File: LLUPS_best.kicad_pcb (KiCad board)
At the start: 2 copper layers, 140 x 90 mm, 39 parts, among them J1 USB_C, J2 Output, J3 Debug, Q1 FS8205A, U1 USBLC6-2SC6, U2 BQ24072, U3 HY2113-KB5B, U4 MT3608, U5 AP2112K-3.3, U6 LN61CN3302MR-G

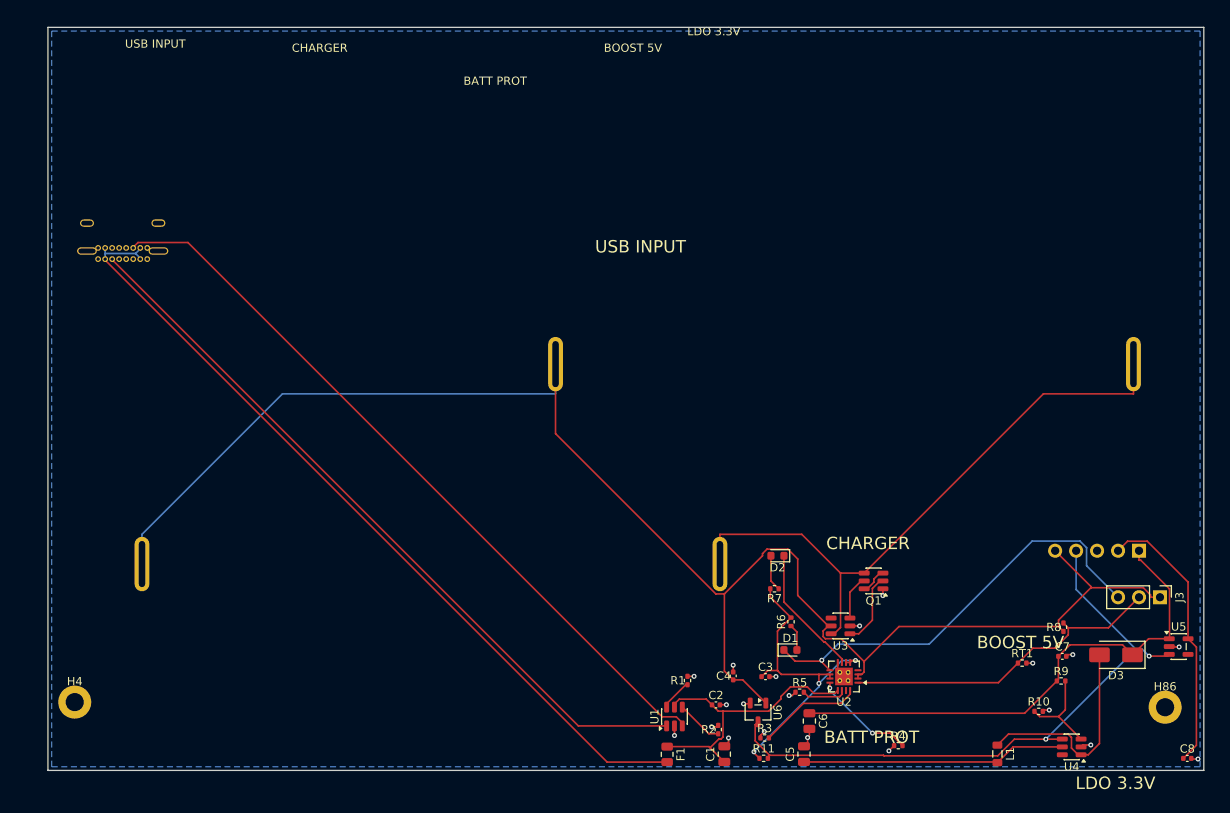
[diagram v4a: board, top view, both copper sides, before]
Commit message: fix: edge connector 180° rotation error on B.Cu (back layer)
When THT connectors are flipped to B.Cu by _assign_layers(), KiCad's
Flip() mirrors the local X-axis. _best_rotation_for_edge() was using
F.Cu outward direction assumptions regardless of layer, causing the
USB connector opening to face inward (toward the board) instead of
outward.

Fix: swap left/right outward angles when comp.layer == Layer.BACK.

Also fix unrelated UnboundLocalError for stop_mid_batch in single-worker
experiment mode.
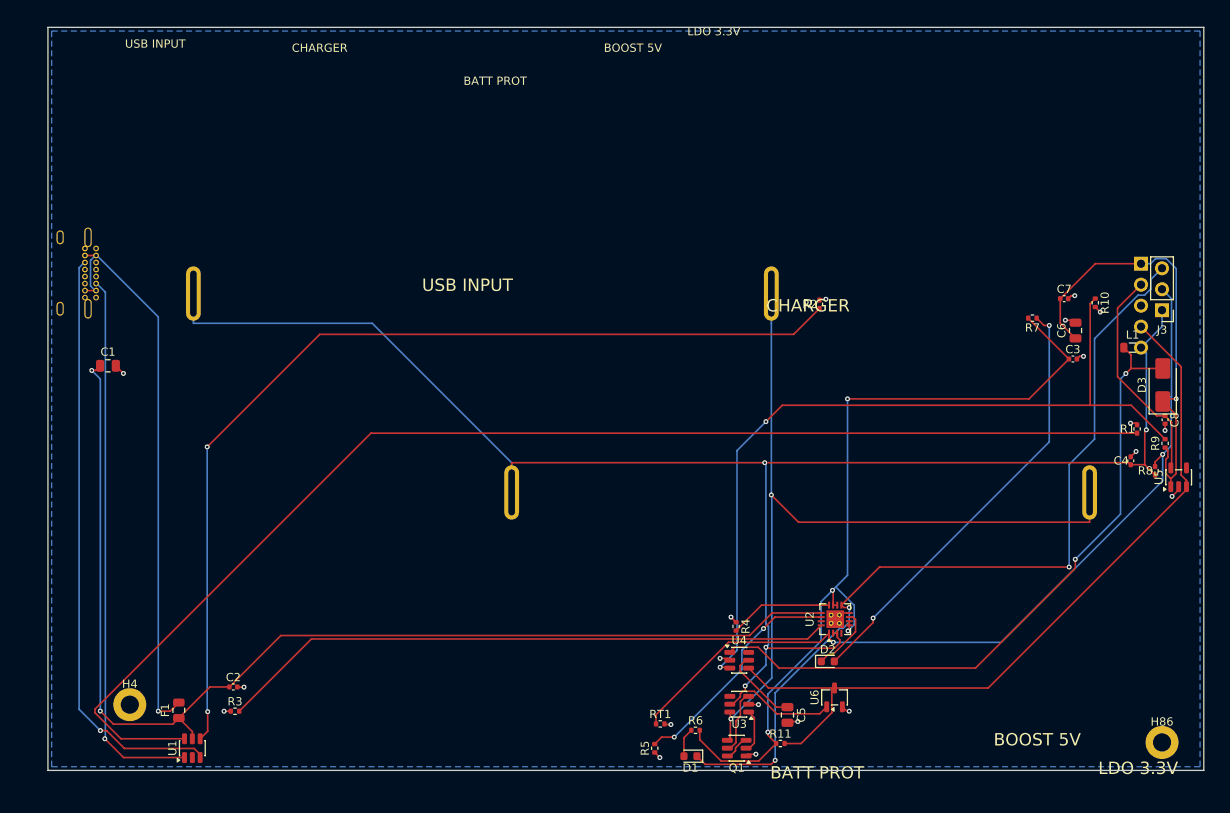
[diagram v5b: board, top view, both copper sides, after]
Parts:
- moved C1 88.2 mm to (7.27, 41.0), turned to 0 degrees
- moved R3 64.2 mm to (22.7, 82.8)
- moved R1 62.4 mm to (131.9, 48.6)
- moved F1 59.4 mm to (15.9, 82.7), turned to 90 degrees
- moved U1 58.5 mm to (17.5, 87.3)
- moved C2 58.5 mm to (22.5, 79.9)
- moved C6 57.2 mm to (124.5, 36.7), turned to 90 degrees
- moved C4 54.8 mm to (131.2, 52.5)
- moved C3 53.5 mm to (124.1, 40.2)
- moved R2 52.9 mm to (93.4, 33.5)
- moved L1 51.9 mm to (131.4, 38.8), turned to 0 degrees
- moved R10 50.0 mm to (126.9, 33.4), turned to -90 degrees
- moved BT2 45.6 mm to (91.2, 56.3)
- moved R7 45.3 mm to (119.2, 35.2)
- moved BT1 44.7 mm to (52.6, 32.2)
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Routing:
- net Net-(R1-Pad1): track 3.89 -> 152.6 mm
- net Net-(R2-Pad1): track 5.69 -> 116.9 mm, vias 0 -> 2
- net /VBUS: track 35.8 -> 139.7 mm, vias 0 -> 2
- net Net-(U4-FB): track 11.7 -> 97.3 mm, vias 0 -> 2
- net /VSYS: track 41.4 -> 104.4 mm, vias 3 -> 4
- net Net-(U2-ISET): track 12.5 -> 74.8 mm
- net /NTC_SENSE: track 39.7 -> 101.5 mm, vias 0 -> 2
- net Net-(D3-A): track 26.0 -> 81.9 mm, vias 0 -> 2
- net /CHG_N: track 52.7 -> 104.4 mm, vias 1 -> 3
- net Net-(D2-A): track 4.39 -> 53.4 mm, vias 0 -> 2
- net Net-(F1-Pad2): track 100.2 -> 68.9 mm, vias 0 -> 1
- net /CELL_NEG: track 76.3 -> 100.8 mm, vias 0 -> 2
- net Net-(J1-CC1): track 90.6 -> 66.3 mm, vias 0 -> 1
- net /VSYS_BOOST: track 32.1 -> 9.49 mm
- net Net-(U2-TMR): track 5.41 -> 27.9 mm, vias 0 -> 2
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
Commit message: feat: hierarchical group-based placement with SMT-opposite-THT scoring
Add two-phase placement strategy: intra-group placement keeps
functionally related components together, then inter-group arrangement
positions groups on the board respecting signal flow order.

Key changes:
- New group_placer.py and groups.py for functional group discovery
  and hierarchical placement
- SMT-opposite-THT and group_coherence scoring metrics (types.py)
- bbox now uses body_center for accurate overlap detection
- GUI toggles for new placement features and stale process cleanup
- Pipeline supports hierarchical mode with flat fallback
- Retuned scoring weights for new metrics
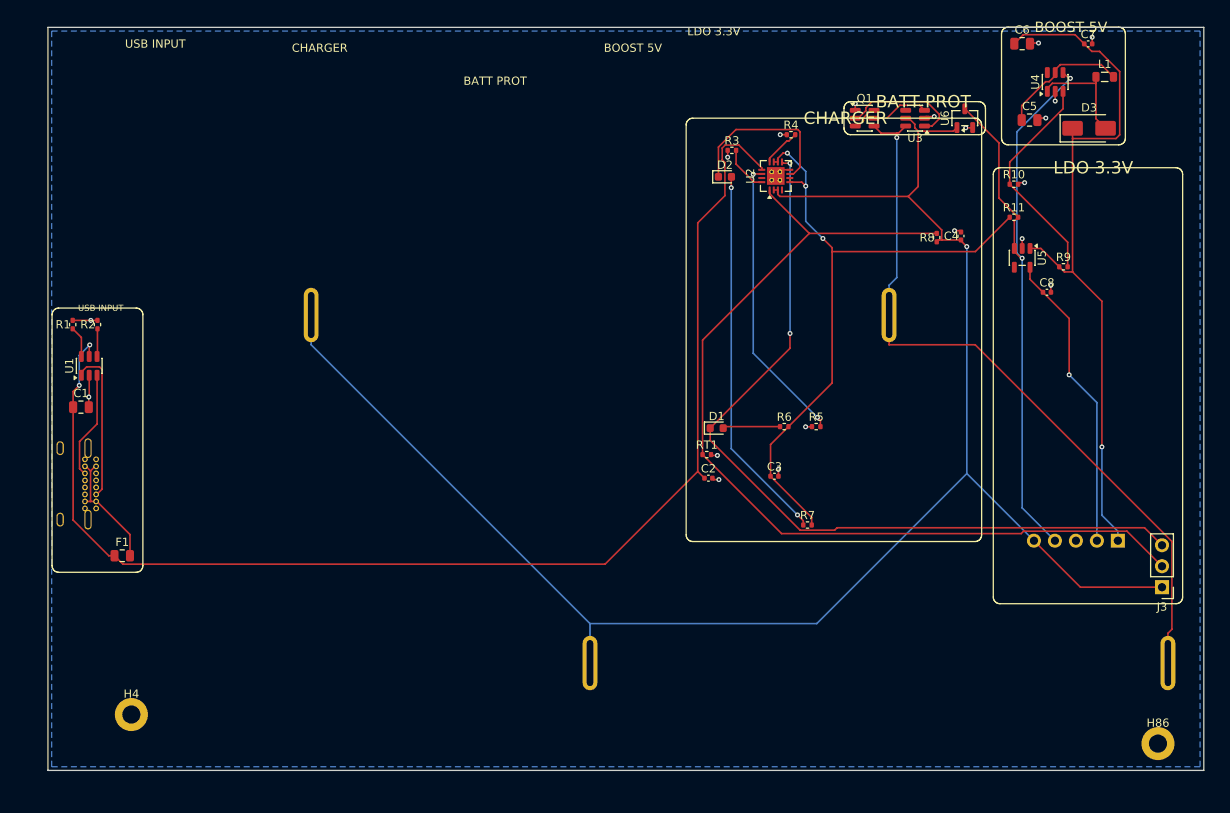
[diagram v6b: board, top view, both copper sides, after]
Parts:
- moved R1 129.5 mm to (3.00, 36.0)
- moved R3 90.8 mm to (82.8, 14.9)
- moved R2 87.5 mm to (6.00, 36.0)
- moved U4 79.8 mm to (122.0, 6.61), turned to 90 degrees
- moved Q1 77.9 mm to (98.9, 11.0), turned to 0 degrees
- moved C5 77.8 mm to (118.9, 11.2), turned to 0 degrees
- moved U3 74.1 mm to (105.0, 11.0)
- moved U6 71.9 mm to (111.1, 11.0)
- moved R11 69.7 mm to (117.0, 23.0)
- moved C2 62.9 mm to (80.0, 54.6)
- moved D2 60.0 mm to (82.0, 18.1)
- moved R4 59.9 mm to (90.0, 13.0), turned to 0 degrees
- moved U2 54.2 mm to (88.2, 18.0)
- moved U1 48.0 mm to (5.00, 41.0)
- moved R5 43.6 mm to (93.1, 48.4), turned to 0 degrees
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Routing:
- net Net-(R1-Pad1): track 152.6 -> 3.79 mm
- net Net-(R2-Pad1): track 116.9 -> 3.37 mm, vias 2 -> 0
- net Net-(U4-FB): track 97.3 -> 26.8 mm, vias 2 -> 0
- net Net-(U2-ISET): track 74.8 -> 5.68 mm
- net Net-(D3-A): track 81.9 -> 13.2 mm, vias 2 -> 0
- net Net-(J1-CC2): track 71.8 -> 13.1 mm, vias 1 -> 0
- net Net-(F1-Pad2): track 68.9 -> 15.2 mm, vias 1 -> 0
- net Net-(J1-CC1): track 66.3 -> 18.8 mm, vias 1 -> 0
- net /5V: track 55.2 -> 87.2 mm
- net /VSYS: track 104.4 -> 80.7 mm, vias 4 -> 3
- net /NTC_SENSE: track 101.5 -> 116.3 mm, vias 2 -> 0
- net /VBUS: track 139.7 -> 154.1 mm
- net /EN: track 96.3 -> 83.2 mm, vias 0 -> 2
- net Net-(D2-K): track 8.01 -> 20.4 mm
- net /CELL_NEG: track 100.8 -> 89.6 mm, vias 2 -> 1
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
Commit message: feat: extract group-label helper and apply labels to GIF frames
Refactor group label application into _apply_group_labels() helper and
call it before rendering baseline and per-round GIF snapshots, so
silkscreen labels appear in progress animations. Update best placement
results from latest experiment run.
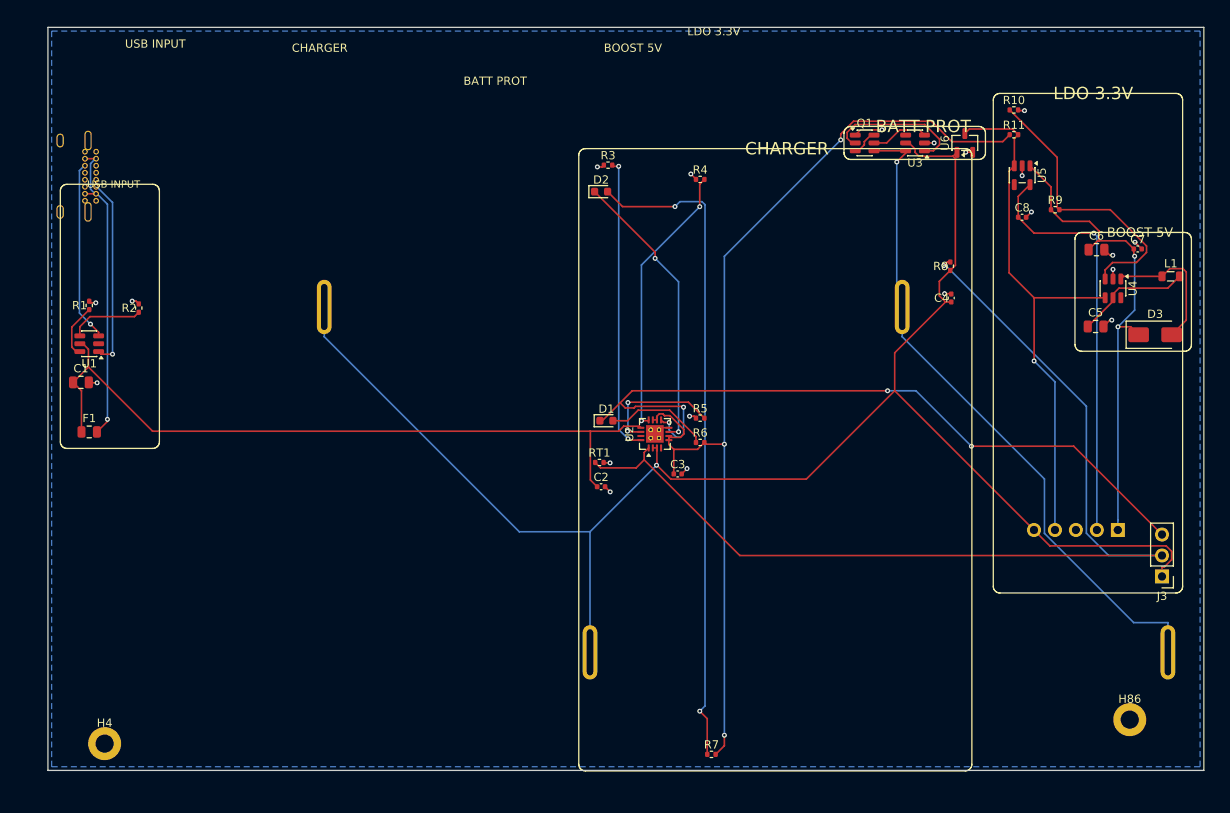
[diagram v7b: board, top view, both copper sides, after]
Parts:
- moved J1 37.3 mm to (5.84, 21.0)
- moved U2 34.5 mm to (73.5, 49.2)
- moved R7 30.1 mm to (80.4, 88.1)
- moved C6 26.5 mm to (127.0, 26.9)
- moved C5 26.2 mm to (126.9, 36.2)
- moved D3 26.2 mm to (134.1, 37.2)
- moved U4 26.0 mm to (129.0, 31.6), turned to -90 degrees
- moved C7 25.6 mm to (132.0, 26.8)
- moved L1 25.4 mm to (136.0, 30.2)
- moved F1 15.5 mm to (5.00, 49.0)
- moved D2 15.1 mm to (67.0, 19.9)
- moved R3 15.1 mm to (67.8, 16.7)
- moved R5 14.1 mm to (79.0, 47.3)
- moved D1 13.4 mm to (67.6, 47.6)
- moved C2 13.0 mm to (67.0, 55.6)
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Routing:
- net /VBUS: track 154.1 -> 90.0 mm, vias 2 -> 0
- net /VSYS: track 80.7 -> 122.9 mm
- net Net-(D2-A): track 45.8 -> 80.2 mm
- net Net-(U2-ISET): track 5.68 -> 35.9 mm, vias 0 -> 2
- net /5V: track 87.2 -> 58.6 mm, vias 1 -> 2
- net Net-(U2-ILIM): track 4.73 -> 33.3 mm, vias 0 -> 2
- net Net-(F1-Pad2): track 15.2 -> 37.6 mm, vias 0 -> 1
- net Net-(U2-TMR): track 35.0 -> 15.2 mm
- net /EN: track 83.2 -> 66.2 mm, vias 2 -> 1
- net /VBAT: track 209.9 -> 193.6 mm
- net /3V3: track 36.5 -> 50.6 mm
- net Net-(D2-K): track 20.4 -> 34.5 mm, vias 0 -> 2
- net /NTC_SENSE: track 116.3 -> 126.8 mm, vias 0 -> 1
- net Net-(J1-CC2): track 13.1 -> 21.9 mm, vias 0 -> 1
- net Net-(U4-FB): track 26.8 -> 34.7 mm
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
